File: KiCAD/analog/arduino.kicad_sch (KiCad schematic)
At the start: 55 parts, among them J12 Screw_Terminal_01x04, J13 Screw_Terminal_01x03, J14 Screw_Terminal_01x05, J2 8P8C_Shielded, J20 Screw_Terminal_01x04, J21 Screw_Terminal_01x02, J22 Screw_Terminal_01x04, J3 Screw_Terminal_01x04, J31 8P8C_Shielded, J32 Screw_Terminal_01x02, J35 8P8C_Shielded, J6 Screw_Terminal_01x02, J7 Screw_Terminal_01x02, J8 Screw_Terminal_01x02, J9 Screw_Terminal_01x02, Q10 2N7000, Q4 2N7000, Q5 2N7000, Q6 2N7000, Q7 2N7000, U17 Adafruit_PCF8575_Breakout, U18 CD14538B, U3 MCP4728

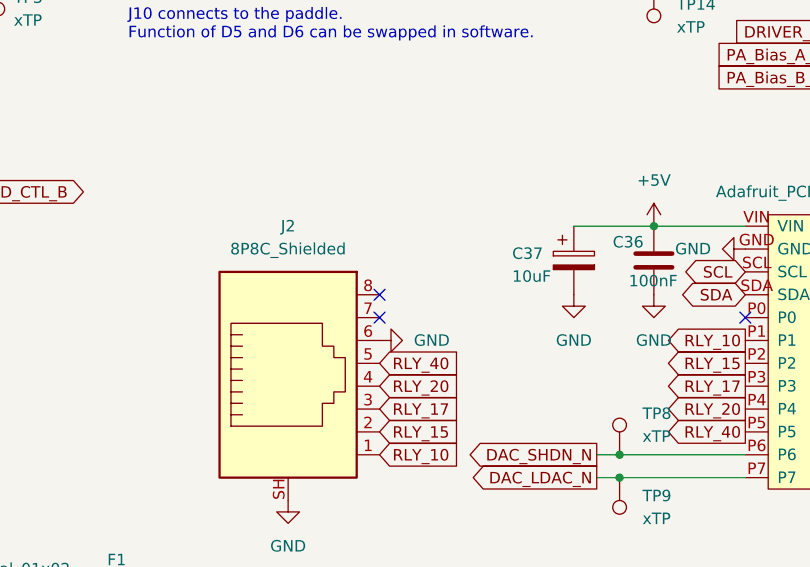
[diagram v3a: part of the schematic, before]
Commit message: revD: Output LPF banks 1-2 pi-pad topology, +28V umbilical from analog
- Output LPF (K5/K6 banks): shared input pi-pad on common rail (R1 100R
  shunt + R2 68R series) feeds the band-select fanout; per-bank
  post-relay shunt (RP9, RP12) at each LPF input to dissipate residual
  bank-to-bank leakage. Banks 3-4 (K1/K2/K7/K8) still pending.
- Output LPF: coil-driver chain for 5 band relays (2N7000 Q1/Q5/Q8-10
  + 1N4148 flyback D7-D11 + screw terminals J16/J25/J26/J27/J29 with
  pin 1=+28V, pin 2=FET drain).
- Analog J2 RJ45 to LPF: pin 8=+28V, pins 6/7/SH=GND, pins 1-5=
  RLY_10/15/17/20/40. Netlist regenerated; +28V and all 5 RLY_xx
  signals resolve on both sides.
- Output LPF project: add sym-lib-table and fp-lib-table pointing at
  ../xmitter.kicad_sym and ../xmitter.pretty (mirrors ss_pa/analog
  convention).

Co-Authored-By: Claude Opus 4.7 <noreply@anthropic.com>
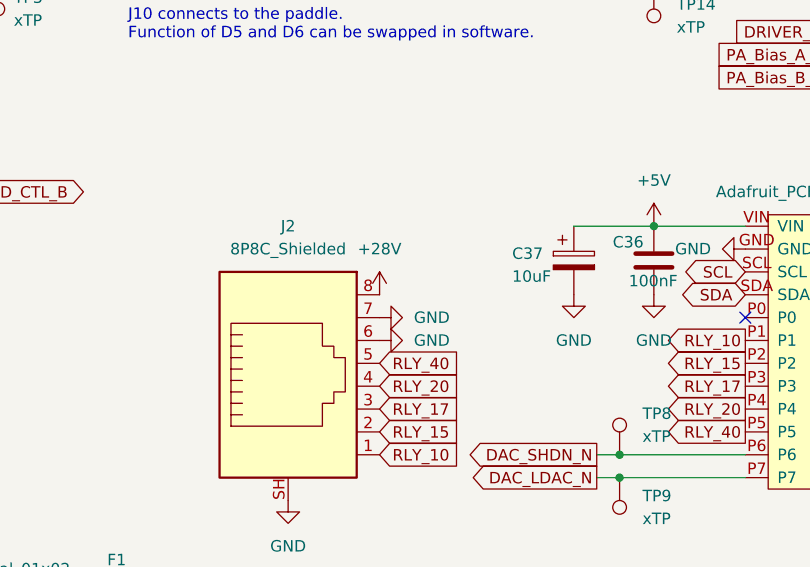
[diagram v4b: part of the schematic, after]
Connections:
- net GND: now also J2.7
- net +28V: now reaches J2.8
- no-connect marks 16 -> 14
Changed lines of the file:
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@@
 	)
 	(no_connect
-		(at 134.62 68.58)
-	)
-	(no_connect
 		(at 59.69 41.91)
 	)
@@
 		(at 167.64 157.48)
 	)
-	(no_connect
-		(at 134.62 66.04)
-	)
 	(wire
 		(pts
@@
 	(symbol
 		(lib_id "power:GND")
+		(at 134.62 68.58 90)
+		(unit 1)
+		(body_style 1)
+		(exclude_from_sim no)
+		(in_bom yes)
+		(on_board yes)
+		(in_pos_files yes)
+		(dnp no)
+		(fields_autoplaced yes)
+		(property "Reference" "#PWR036"
+			(at 140.97 68.58 0)
+			(hide yes)
+			(show_name no)
+			(do_not_autoplace no)
+			(effects
+				(font
+					(size 1.27 1.27)
+				)
+			)
+		)
+		(property "Value" "GND"
+			(at 138.43 68.5799 90)
+			(show_name no)
+			(do_not_autoplace no)
+			(effects
+				(font
+					(size 1.27 1.27)
+				)
+				(justify right)
+			)
+		)
+		(property "Footprint" ""
+			(at 134.62 68.58 0)
+			(hide yes)
+			(show_name no)
+			(do_not_autoplace no)
+			(effects
+				(font
+					(size 1.27 1.27)
+				)
+			)
+		)
+		(property "Datasheet" ""
+			(at 134.62 68.58 0)
+			(hide yes)
+			(show_name no)
+			(do_not_autoplace no)
+			(effects
+				(font
+					(size 1.27 1.27)
+				)
+			)
+		)
+		(property "Description" "Power symbol creates a global label with name \"GND\" , ground"
+			(at 134.62 68.58 0)
+			(hide yes)
+			(show_name no)
+			(do_not_autoplace no)
+			(effects
+				(font
+					(size 1.27 1.27)
+				)
+			)
+		)
+		(pin "1"
+		)
+		(instances
+			(project "analog"
+				(path "/d3de40b8-856b-4fbd-829c-f45ffcd55742/2d83d0b5-86d4-4ced-ab68-6465e3dc2d72"
+					(reference "#PWR036")
+					(unit 1)
+				)
+			)
+		)
+	)
+	(symbol
+		(lib_id "power:GND")
 		(at 124.46 88.9 0)
 		(unit 1)
@@
 					(unit 1)
 				)
+			)
+		)
+	)
+	(symbol
+		(lib_id "power:+28V")
+		(at 134.62 66.04 0)
+		(unit 1)
+		(body_style 1)
+		(exclude_from_sim no)
+		(in_bom yes)
+		(on_board yes)
+		(in_pos_files yes)
+		(dnp no)
+		(fields_autoplaced yes)
+		(property "Reference" "#PWR037"
+			(at 134.62 69.85 0)
+			(hide yes)
+			(show_name no)
+			(do_not_autoplace no)
+			(effects
+				(font
+					(size 1.27 1.27)
+				)
+			)
+		)
+		(property "Value" "+28V"
+			(at 134.62 60.96 0)
+			(show_name no)
+			(do_not_autoplace no)
+			(effects
+				(font
+					(size 1.27 1.27)
+				)
+			)
+		)
+		(property "Footprint" ""
+			(at 140.97 64.77 0)
+			(hide yes)
+			(show_name no)
+			(do_not_autoplace no)
+			(effects
+				(font
+					(size 1.27 1.27)
+				)
+			)
+		)
+		(property "Datasheet" ""
+			(at 140.97 64.77 0)
+			(hide yes)
+			(show_name no)
+			(do_not_autoplace no)
+			(effects
+				(font
+					(size 1.27 1.27)
+				)
+			)
+		)
+		(property "Description" "Power symbol creates a global label with name \"+28V\""
+			(at 134.62 66.04 0)
+			(hide yes)
+			(show_name no)
+			(do_not_autoplace no)
+			(effects
+				(font
+					(size 1.27 1.27)
+				)
+			)
+		)
+		(pin "1"
+		)
+		(instances
+			(project "analog"
+				(path "/d3de40b8-856b-4fbd-829c-f45ffcd55742/2d83d0b5-86d4-4ced-ab68-6465e3dc2d72"
+					(reference "#PWR037")
+					(unit 1)
+				)

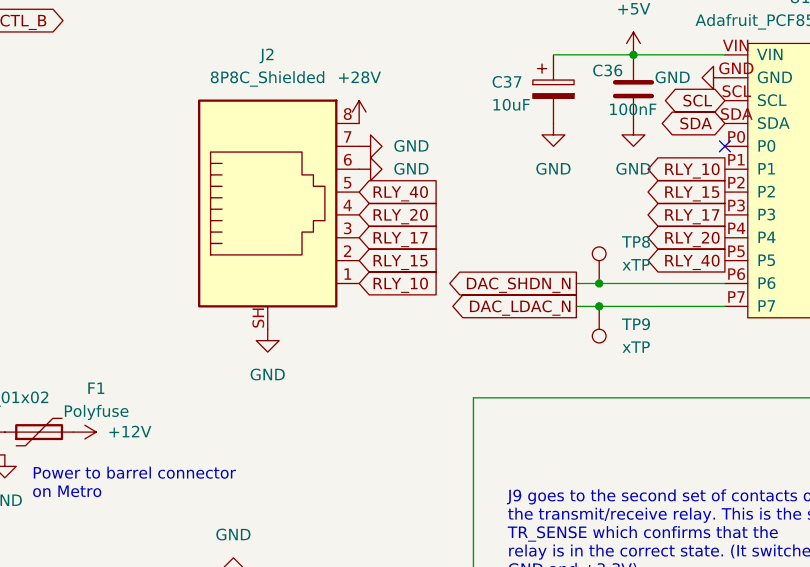
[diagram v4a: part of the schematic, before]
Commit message: WIP revD Output LPF: 10m bank converted to G6K DPDT, library additions
Intermediate snapshot -- migration in progress.

- xmitter library: add Relay_G6K symbol (copied from stock KiCad
  Relay:G6K-2, pre-linked to xmitter:Relay_DPDT_G6K-2P-Y-T1 footprint)
  and Relay_DPDT_G6K-2P-Y-T1.kicad_mod footprint (10 x 6.5 mm body,
  -Y pitch: 3.2mm/2.2mm/2.2mm along row, 5.08mm row spacing, 0.85mm
  THT holes)
- Documentation/Components: Omron G6K-T1 datasheet
- Output LPF 10m bank: converted from K1+K8 SPST pair to single K1
  DPDT G6K. Pole 1 switches output (pin 3=COM to LPF-out, pin 4=NO
  to common J1). Pole 2 switches input (pin 6=COM to LPF-in, pin
  5=NO to common J28). K8 removed.
- Analog: WIP (details TBD when more banks converted)

Known open items before next commit:
- +12V net on LPF has no source (umbilical still carries +28V, needs
  rewire or LDO)
- 40m/20m/17m/15m banks still on old RSS-SR042P SPST topology
- Consider moving R3 to K1 pin 7 (removes 0.4 dB active-path loss,
  keeps swamp function via NC path when bank unselected)

Co-Authored-By: Claude Opus 4.7 <noreply@anthropic.com>
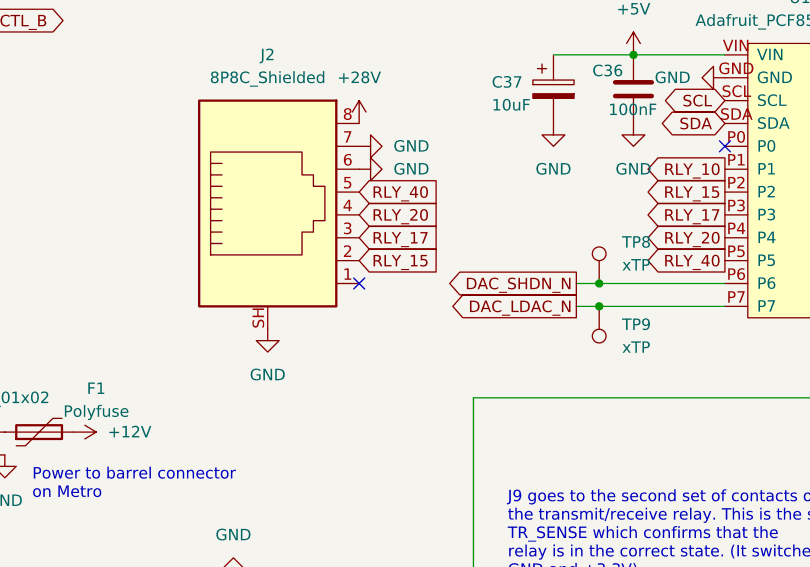
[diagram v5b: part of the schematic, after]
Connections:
- net RLY_10: no longer J2.1
- no-connect marks 14 -> 15
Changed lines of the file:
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@@
+	)
+	(no_connect
+		(at 134.62 83.82)
 	)
 	(no_connect
@@
 			(hide yes)
 			(show_name no)
-			(do_not_autoplace no)
-			(effects
-				(font
-					(size 1.27 1.27)
-				)
-				(justify left)
-			)
-		)
-	)
-	(global_label "RLY_10"
-		(shape input)
-		(at 134.62 83.82 0)
-		(fields_autoplaced yes)
-		(effects
-			(font
-				(size 1.27 1.27)
-			)
-			(justify left)
-		)
-		(property "Intersheetrefs" "${INTERSHEET_REFS}"
-			(at 144.3785 83.82 0)
-			(hide yes)
-			(show_name no)

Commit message: revD: drop 10m, convert LPF to DPDT G6K throughout, retire +28V rail
Output LPF:
- 10m bank removed (K8/K1-equivalent, L15/L16/L17, CF14-CF25 and
  parallel-cap combos, R4 original). 10m to be handled via main rig.
- All 4 remaining bands now use a single xmitter:Relay_G6K DPDT per
  bank (K1=15m, K2=17m, K3=20m, K4=40m). Pole 1 switches output,
  Pole 2 switches input. Half the relay count vs the old SPST pair.
- Coil chain per bank: pin1=+12V, pin8=RLY_xx_DRIVE via 2N7000
  (Q5/Q8/Q1/Q10 for 15/17/20/40) with 1N4148 flyback (D7/D8/D9/D11).
- Swamp resistors (R2-R9, 2 per bank) placed on relay pin 7 (NC) so
  they only load the LPF when the bank is unselected -- removes
  active-path insertion loss.
- Legacy screw terminals J16/J25/J26/J27/J29 and +28V coil feed
  deleted. Umbilical now carries +12V on J2 pin 8.

Analog:
- LT1054 +28V voltage doubler (U9) and its support caps/diodes
  removed. +28V net purged from every sheet.
- +12V (LM2940CT-12 U8) now feeds the LPF coil supply via J2 pin 8.
- LT1054 -12V inverter (U7) retained for LM7171 negative rail.
- +12V current budget: ~75-100 mA worst case (op-amp rails + one
  G6K coil active) against 1 A LDO capacity.

Co-Authored-By: Claude Opus 4.7 <noreply@anthropic.com>
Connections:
- net +28V is gone; now on net +12V: J2.8
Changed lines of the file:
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@@
-	)
-	(symbol
-		(lib_id "power:+28V")
-		(at 134.62 66.04 0)
-		(unit 1)
-		(body_style 1)
-		(exclude_from_sim no)
-		(in_bom yes)
-		(on_board yes)
-		(in_pos_files yes)
-		(dnp no)
-		(fields_autoplaced yes)
-		(property "Reference" "#PWR037"
-			(at 134.62 69.85 0)
-			(hide yes)
-			(show_name no)
-			(do_not_autoplace no)
-			(effects
-				(font
-					(size 1.27 1.27)
-				)
-			)
-		)
-		(property "Value" "+28V"
-			(at 134.62 60.96 0)
-			(show_name no)
-			(do_not_autoplace no)
-			(effects
-				(font
-					(size 1.27 1.27)
-				)
-			)
-		)
-		(property "Footprint" ""
-			(at 140.97 64.77 0)
-			(hide yes)
-			(show_name no)
-			(do_not_autoplace no)
-			(effects
-				(font
-					(size 1.27 1.27)
-				)
-			)
-		)
-		(property "Datasheet" ""
-			(at 140.97 64.77 0)
-			(hide yes)
-			(show_name no)
-			(do_not_autoplace no)
-			(effects
-				(font
-					(size 1.27 1.27)
-				)
-			)
-		)
-		(property "Description" "Power symbol creates a global label with name \"+28V\""
-			(at 134.62 66.04 0)
-			(hide yes)
-			(show_name no)
-			(do_not_autoplace no)
-			(effects
-				(font
-					(size 1.27 1.27)
-				)
-			)
-		)
-		(pin "1"
-		)
-		(instances
-			(project "analog"
-				(path "/d3de40b8-856b-4fbd-829c-f45ffcd55742/2d83d0b5-86d4-4ced-ab68-6465e3dc2d72"
-					(reference "#PWR037")
-					(unit 1)
-				)
-			)
-		)
 	)
 	(symbol
@@
 					(unit 1)
 				)
+			)
+		)
+	)
+	(symbol
+		(lib_id "power:+12V")
+		(at 134.62 66.04 270)
+		(unit 1)
+		(body_style 1)
+		(exclude_from_sim no)
+		(in_bom yes)
+		(on_board yes)
+		(in_pos_files yes)
+		(dnp no)
+		(fields_autoplaced yes)
+		(property "Reference" "#PWR037"
+			(at 130.81 66.04 0)
+			(hide yes)
+			(show_name no)
+			(do_not_autoplace no)
+			(effects
+				(font
+					(size 1.27 1.27)
+				)
+			)
+		)
+		(property "Value" "+12V"
+			(at 138.43 66.0399 90)
+			(show_name no)
+			(do_not_autoplace no)
+			(effects
+				(font
+					(size 1.27 1.27)
+				)
+				(justify left)
+			)
+		)
+		(property "Footprint" ""
+			(at 134.62 66.04 0)
+			(hide yes)
+			(show_name no)
+			(do_not_autoplace no)
+			(effects
+				(font
+					(size 1.27 1.27)
+				)
+			)
+		)
+		(property "Datasheet" ""
+			(at 134.62 66.04 0)
+			(hide yes)
+			(show_name no)
+			(do_not_autoplace no)
+			(effects
+				(font
+					(size 1.27 1.27)
+				)
+			)
+		)
+		(property "Description" "Power symbol creates a global label with name \"+12V\""
+			(at 134.62 66.04 0)
+			(hide yes)
+			(show_name no)
+			(do_not_autoplace no)
+			(effects
+				(font
+					(size 1.27 1.27)
+				)
+			)
+		)
+		(pin "1"
+		)
+		(instances
+			(project "analog"
+				(path "/d3de40b8-856b-4fbd-829c-f45ffcd55742/2d83d0b5-86d4-4ced-ab68-6465e3dc2d72"
+					(reference "#PWR037")
+					(unit 1)
+				)

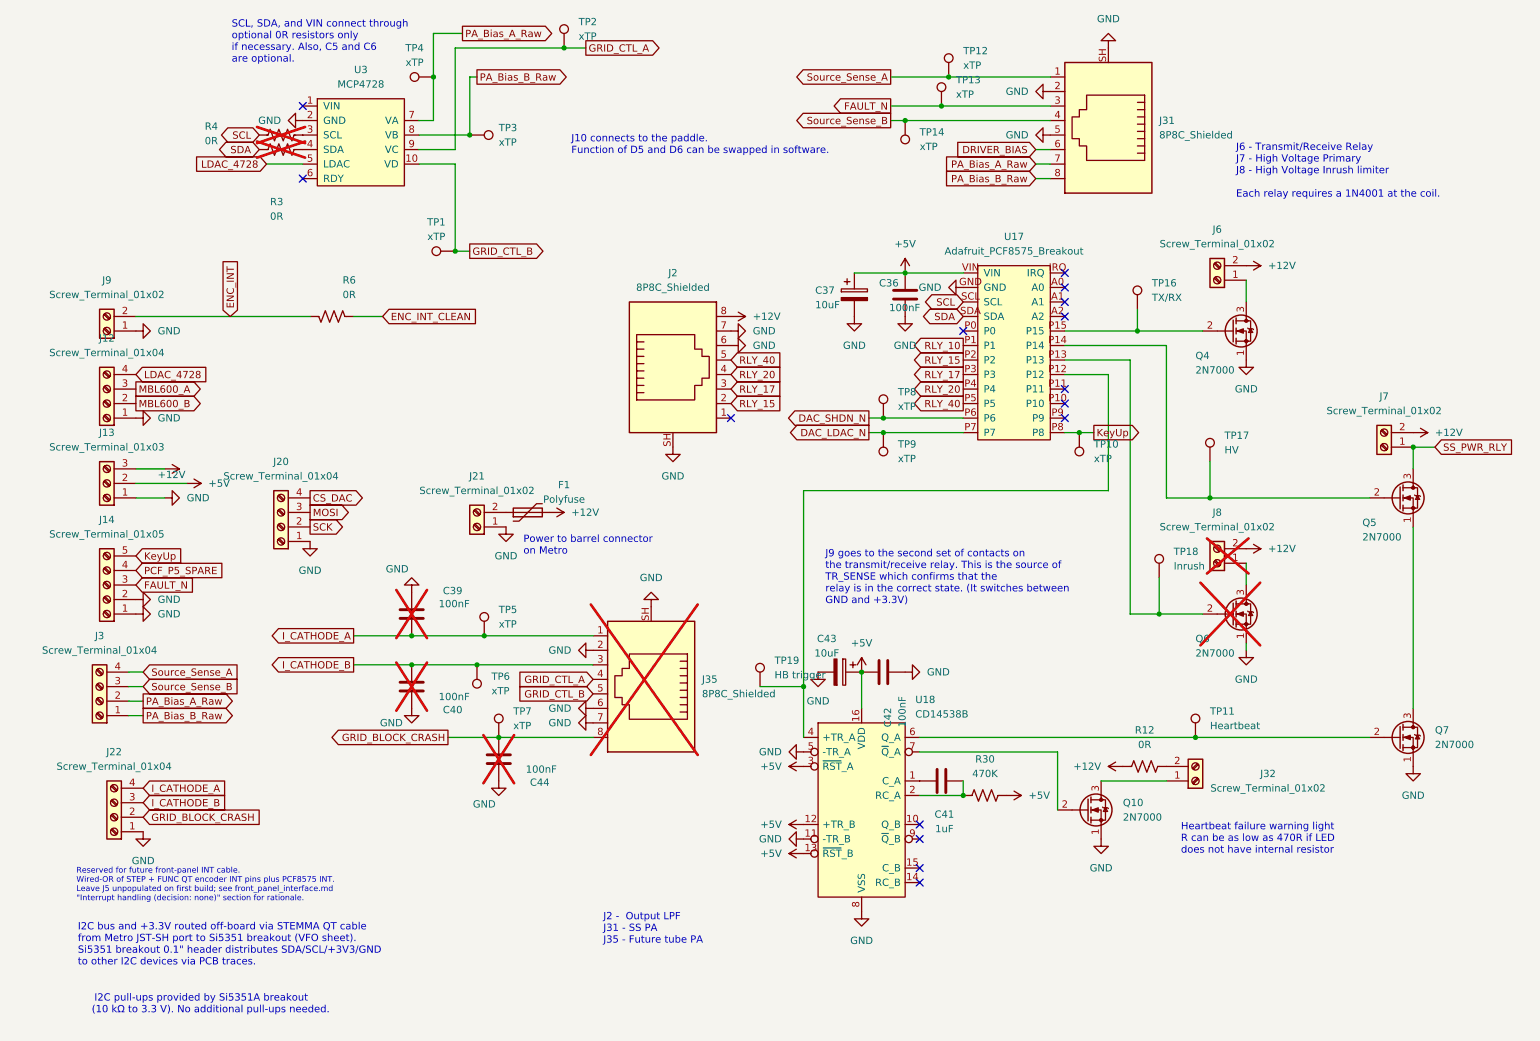
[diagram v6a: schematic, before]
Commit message: revD: ss_pa Option C 5V rail + analog SW1 THT + R/C footprints + doc refresh
ss_pa Option C: swap U13 to LM2936Z-5.0 (full +5V logic rail), re-size
R10 10K->6.8K to preserve ~0.3V fault trip at new rail, drop +3.3V net
entirely. Fixes the previously-dead +5V bus that had no source.

Analog SW1 (Si5351 bringup DPDT): swap SMD footprint for
Button_Switch_THT:SW_CK_JS202011CQN_DPDT_Straight. Verified pin-numbering
convention (pin 1 above pin 6 in THT) matches user's intended DPST
wiring; both SDA/SCL break together.

Analog: assign missing footprints to R3/R4/R5/R8/R9 (DIN0207 axial) and
C4/C5/C6/C7/C8 (disc ceramic 5mm). Add xmitter:DIP-14_W7.62mm.kicad_mod
and 74HCT125 symbol to the xmitter library.

Documentation: Rev D handoff doc updated with M1-M8 fix status, Option C
notes, I2C bus voltage architecture, 74HCT125 SPI shifter, FAULT_N
divider details, and Metro-no-footprint note. Supporting docs updated:
i2c_bus.md full rewrite for 5V HV bus + STEMMA reroute, revD_interconnect
board inventory refresh, status banners on ss_pa.md / Master_Description /
cw_envelope_keyer / front_panel_interface pointing to handoff doc for
items beyond their last-current date.

Co-Authored-By: Claude Opus 4.7 <noreply@anthropic.com>
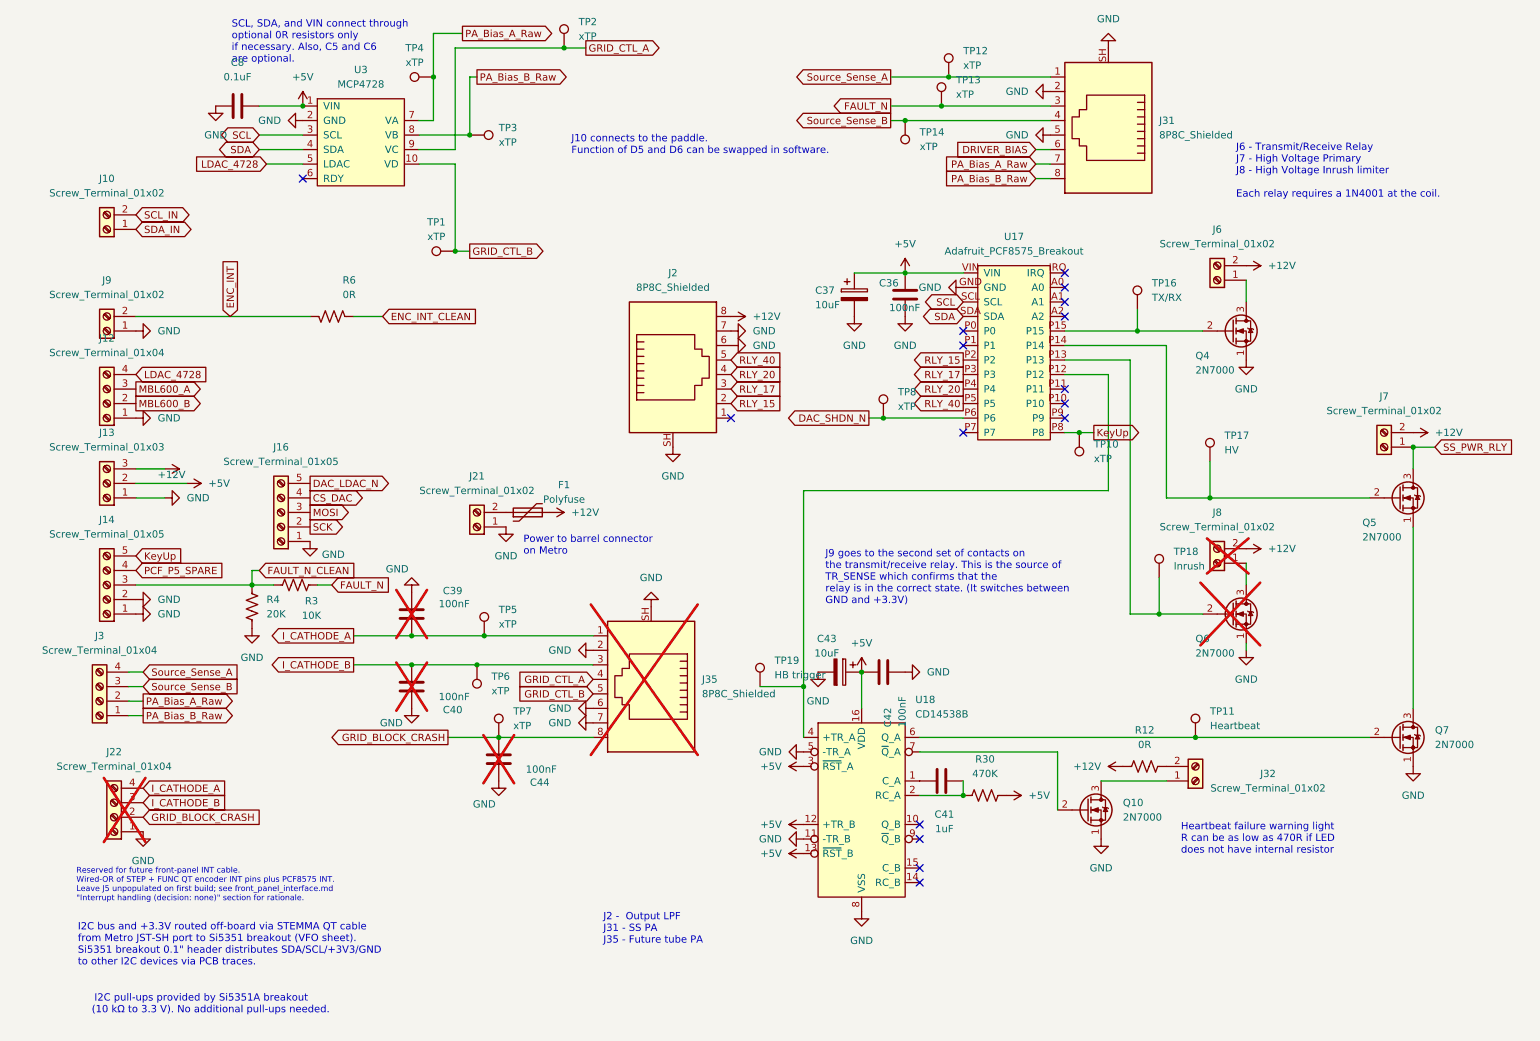
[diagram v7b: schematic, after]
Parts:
- removed J20: Screw_Terminal_01x04, TerminalBlock_Phoenix:TerminalBlock_Phoenix_MKDS-1,5-4_1x04_P5.00mm_Horizontal, symbol Connector:Screw_Terminal_01x04
- removed TP9: xTP, Connector_PinHeader_2.54mm:PinHeader_1x01_P2.54mm_Vertical, symbol xmitter:xTP
- added C8: 0.1uF, Capacitor_THT:C_Disc_D5.0mm_W2.5mm_P5.00mm, symbol Device:C
- added J10: Screw_Terminal_01x02, TerminalBlock_Phoenix:TerminalBlock_Phoenix_MKDS-1,5-2_1x02_P5.00mm_Horizontal, symbol Connector:Screw_Terminal_01x02
- added J16: Screw_Terminal_01x05, TerminalBlock_Phoenix:TerminalBlock_Phoenix_MKDS-1,5-5_1x05_P5.00mm_Horizontal, symbol Connector:Screw_Terminal_01x05
- J22: now not fitted
- R3: value 0R -> 10K; now fitted
- R4: value 0R -> 20K; now fitted
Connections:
- net +5V: now also U3.1 (VIN), C8.2
- net CS_DAC: now also J16.4 (Pin_4)
- net DAC_LDAC_N: now also J16.5 (Pin_5); no longer U17.P7
- net FAULT_N: now also R3.2; no longer J14.3 (Pin_3)
- net GND: now also R4.2, C8.1, J16.1 (Pin_1)
- net MOSI: now also J16.3 (Pin_3)
- net SCK: now also J16.2 (Pin_2)
- net SCL: now also U3.3 (SCL); no longer R4.1
- net SDA: now also U3.4 (SDA); no longer R3.1
- net RLY_10: no longer names the net of U17.P1
- new net FAULT_N_CLEAN: J14.3 (Pin_3), R3.1, R4.1
- new net SCL_IN: J10.2 (Pin_2)
- new net SDA_IN: J10.1 (Pin_1)
- no-connect marks 15 -> 16
